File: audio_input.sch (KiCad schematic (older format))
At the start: 17 parts, among them U8 OPA1664

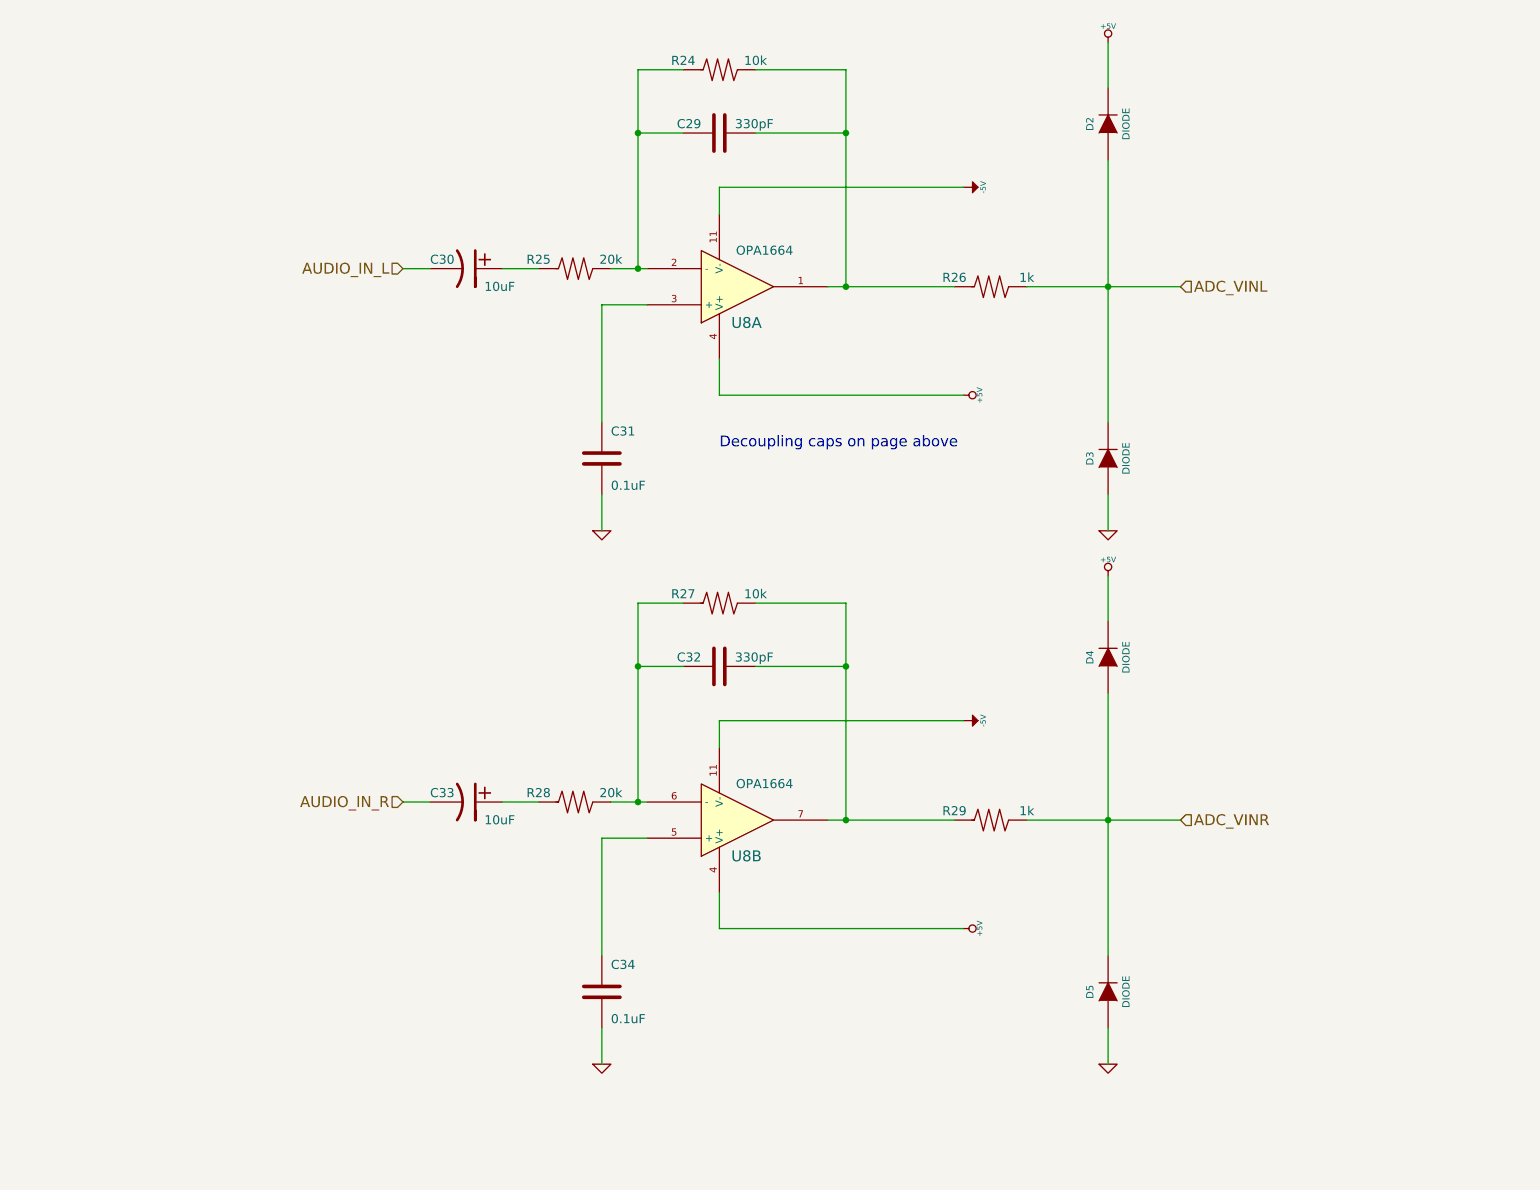
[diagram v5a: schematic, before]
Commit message: Fixed decoupling cap polarity on output op-amp, added bias to analog input, changed capacitor footprints to reflect new capacitor selections
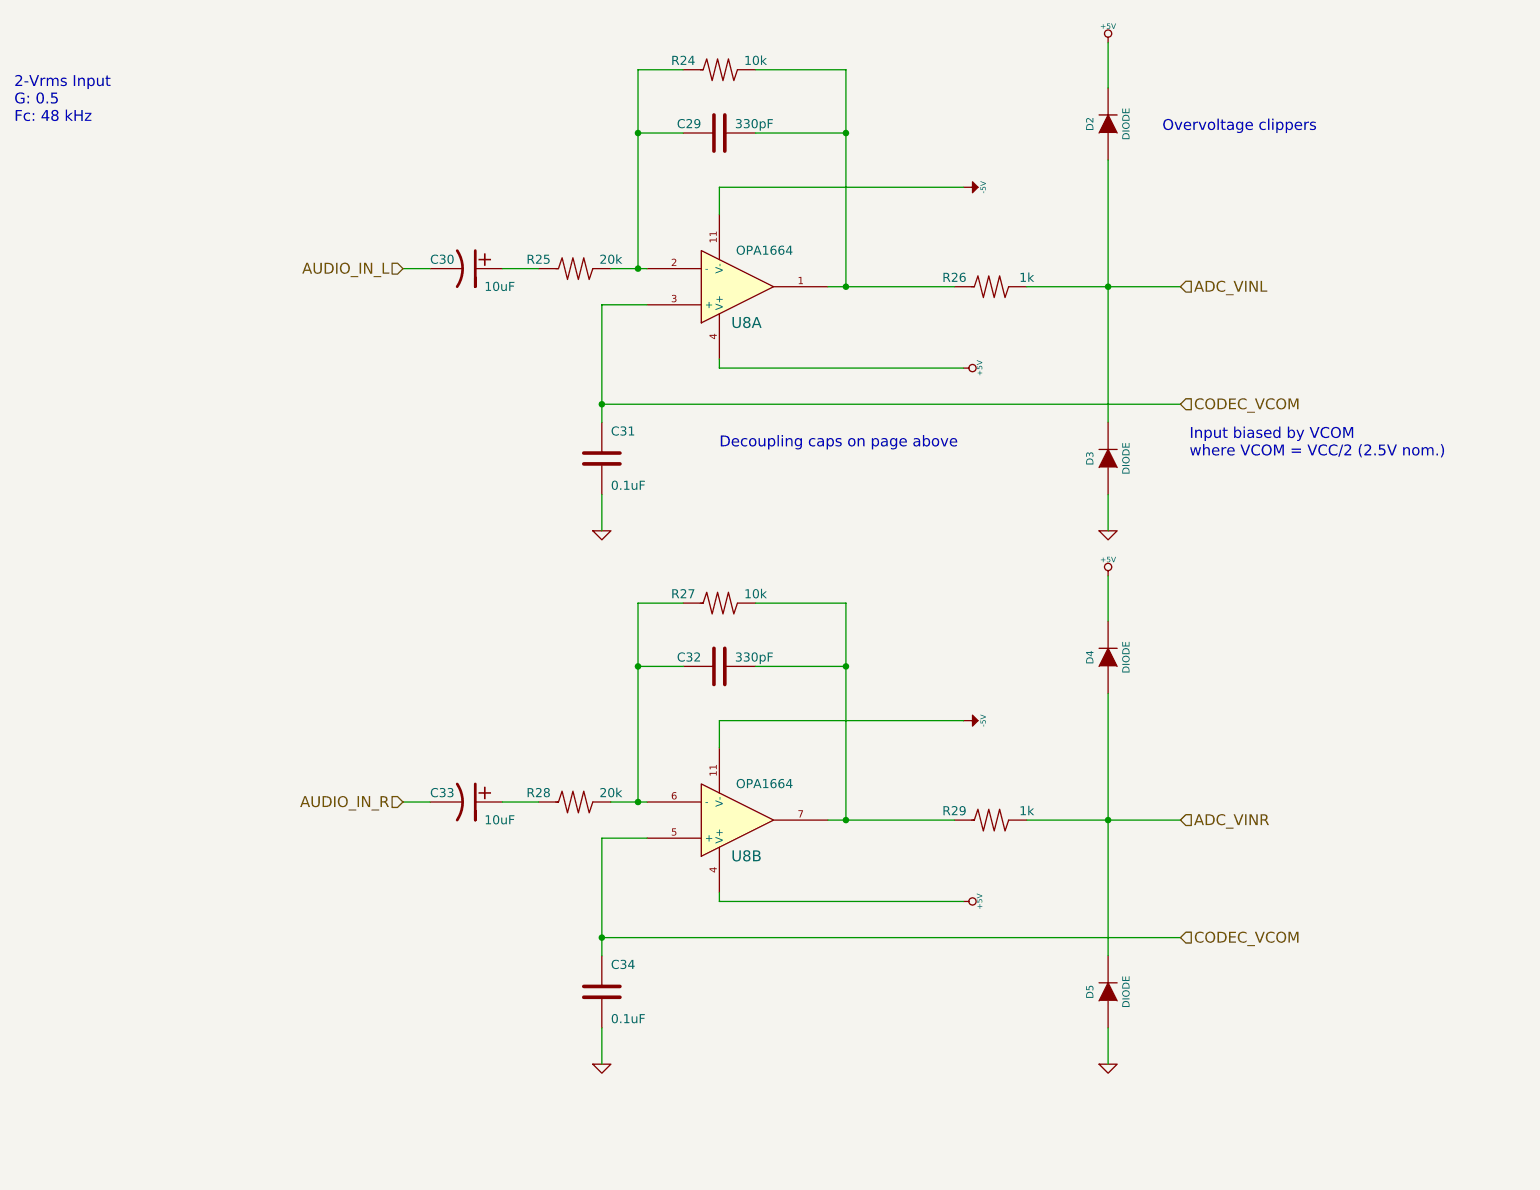
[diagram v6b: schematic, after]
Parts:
- C30, C33: footprint (none) -> Capacitors_SMD:c_elec_6.3x5.7
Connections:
- net CODEC_VCOM: now reaches C31.1, U8.3 (+)
- net CODEC_VCOM: now also C34.1, U8.5 (+)
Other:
- note added: "2-Vrms Input\nG: 0.5\nFc: 48 kHz"
- note added: "Input biased by VCOM \nwhere VCOM = VCC/2 (2.5V nom.)"
- note added: "Overvoltage clippers"
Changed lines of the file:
@@
 	1    0    0    1
 $EndComp
-Wire Wire Line
-	3250 2000 3400 2000
-Wire Wire Line
-	4400 2000 4600 2000
-Wire Wire Line
-	5000 1550 5000 1700
-$Comp
-L -5V #PWR88
+$Comp
+L -5V #PWR087
 U 1 1 5A49B7EA
 P 6350 1550
-F 0 "#PWR88" H 6350 1690 20  0001 C CNN
+F 0 "#PWR087" H 6350 1690 20  0001 C CNN
 F 1 "-5V" H 6350 1660 30  0000 C CNN
 F 2 "" H 6350 1550 60  0000 C CNN
@@
 	0    -1   -1   0
 $EndComp
-Wire Wire Line
-	4550 900  4550 2000
-Wire Wire Line
-	4550 1250 4800 1250
-Connection ~ 4550 2000
 $Comp
 L CP1 C30
@@
 F 0 "C30" V 3550 1800 50  0000 L CNN
 F 1 "10uF" V 3700 2100 50  0000 L CNN
-F 2 "" H 3600 2000 60  0001 C CNN
+F 2 "Capacitors_SMD:c_elec_6.3x5.7" H 3600 2000 60  0001 C CNN
 F 3 "" H 3600 2000 60  0000 C CNN
 	1    3600 2000
@@
 	1    0    0    -1
 $EndComp
-Wire Wire Line
-	4350 2850 4350 2200
-Wire Wire Line
-	4350 2200 4600 2200
-Wire Wire Line
-	5000 1550 6350 1550
-Wire Wire Line
-	5600 2100 6300 2100
-Wire Wire Line
-	5700 900  5700 2100
-Wire Wire Line
-	5700 1250 5200 1250
 $Comp
 L R R24
@@
 	1    0    0    -1
 $EndComp
-Wire Wire Line
-	4550 900  4800 900
-Connection ~ 4550 1250
-Wire Wire Line
-	5200 900  5700 900
-Connection ~ 5700 1250
-$Comp
-L GND #PWR90
+$Comp
+L GND #PWR088
 U 1 1 5A49BD8E
 P 4350 3450
-F 0 "#PWR90" H 4350 3450 30  0001 C CNN
+F 0 "#PWR088" H 4350 3450 30  0001 C CNN
 F 1 "GND" H 4350 3380 30  0001 C CNN
 F 2 "" H 4350 3450 60  0000 C CNN
@@
 	1    0    0    -1
 $EndComp
-Wire Wire Line
-	4350 3450 4350 3450
-Wire Wire Line
-	4350 3450 4350 3250
 $Comp
 L R R25
@@
 	1    0    0    -1
 $EndComp
-Wire Wire Line
-	4000 2000 3800 2000
 $Comp
 L R R26
@@
 	1    0    0    -1
 $EndComp
-Connection ~ 5700 2100
-Connection ~ 7150 2100
-Wire Wire Line
-	6700 2100 7550 2100
-Wire Wire Line
-	7150 1400 7150 2850
-Wire Wire Line
-	7150 750  7150 1000
-Wire Wire Line
-	7150 3450 7150 3250
-$Comp
-L GND #PWR91
+$Comp
+L GND #PWR089
 U 1 1 5A49C264
 P 7150 3450
-F 0 "#PWR91" H 7150 3450 30  0001 C CNN
+F 0 "#PWR089" H 7150 3450 30  0001 C CNN
 F 1 "GND" H 7150 3380 30  0001 C CNN
 F 2 "" H 7150 3450 60  0000 C CNN
@@
 $EndComp
 $Comp
-L +5V #PWR87
+L +5V #PWR090
 U 1 1 5A49C8EC
 P 7150 750
-F 0 "#PWR87" H 7150 840 20  0001 C CNN
+F 0 "#PWR090" H 7150 840 20  0001 C CNN
 F 1 "+5V" H 7150 840 30  0000 C CNN
 F 2 "" H 7150 750 60  0000 C CNN
@@
 	1    0    0    1
 $EndComp
-Wire Wire Line
-	3250 4950 3400 4950
-Wire Wire Line
-	4400 4950 4600 4950
-Wire Wire Line
-	5000 4500 5000 4650
-$Comp
-L -5V #PWR93
+$Comp
+L -5V #PWR091
 U 1 1 5A49EA7F
 P 6350 4500
-F 0 "#PWR93" H 6350 4640 20  0001 C CNN
+F 0 "#PWR091" H 6350 4640 20  0001 C CNN
 F 1 "-5V" H 6350 4610 30  0000 C CNN
 F 2 "" H 6350 4500 60  0000 C CNN
@@
 $EndComp
 $Comp
-L +5V #PWR94
+L +5V #PWR092
 U 1 1 5A49EA85
-P 6350 5650
-F 0 "#PWR94" H 6350 5740 20  0001 C CNN
-F 1 "+5V" H 6350 5740 30  0000 C CNN
-F 2 "" H 6350 5650 60  0000 C CNN
-F 3 "" H 6350 5650 60  0000 C CNN
-	1    6350 5650
+P 6350 5500
+F 0 "#PWR092" H 6350 5590 20  0001 C CNN
+F 1 "+5V" H 6350 5590 30  0000 C CNN
+F 2 "" H 6350 5500 60  0000 C CNN
+F 3 "" H 6350 5500 60  0000 C CNN
+	1    6350 5500
 	0    1    1    0
 $EndComp
@@
 	0    -1   -1   0
 $EndComp
-Wire Wire Line
-	4550 3850 4550 4950
-Wire Wire Line
-	4550 4200 4800 4200
-Connection ~ 4550 4950
 $Comp
 L CP1 C33
@@
 F 0 "C33" V 3550 4750 50  0000 L CNN
 F 1 "10uF" V 3700 5050 50  0000 L CNN
-F 2 "" H 3600 4950 60  0001 C CNN
+F 2 "Capacitors_SMD:c_elec_6.3x5.7" H 3600 4950 60  0001 C CNN
 F 3 "" H 3600 4950 60  0000 C CNN
 	1    3600 4950
@@
 	1    0    0    -1
 $EndComp
-Wire Wire Line
-	4350 5800 4350 5150
-Wire Wire Line
-	4350 5150 4600 5150
-Wire Wire Line
-	5000 5650 6350 5650
-Wire Wire Line
-	5000 4500 6350 4500
-Wire Wire Line
-	5600 5050 6300 5050
-Wire Wire Line
-	5700 3850 5700 5050
-Wire Wire Line
-	5700 4200 5200 4200
 $Comp
 L R R27
@@
 	1    0    0    -1
 $EndComp
-Wire Wire Line
-	4550 3850 4800 3850
-Connection ~ 4550 4200
-Wire Wire Line
-	5200 3850 5700 3850
-Connection ~ 5700 4200
-$Comp
-L GND #PWR95
+$Comp
+L GND #PWR093
 U 1 1 5A49EAC6
 P 4350 6400
-F 0 "#PWR95" H 4350 6400 30  0001 C CNN
+F 0 "#PWR093" H 4350 6400 30  0001 C CNN
 F 1 "GND" H 4350 6330 30  0001 C CNN
 F 2 "" H 4350 6400 60  0000 C CNN
@@
 	1    0    0    -1
 $EndComp
-Wire Wire Line
-	4350 6400 4350 6400
-Wire Wire Line
-	4350 6400 4350 6200
 $Comp
 L R R28
@@
 	1    0    0    -1
 $EndComp
-Wire Wire Line
-	4000 4950 3800 4950
 $Comp
 L R R29
@@
 	1    0    0    -1
 $EndComp
-Connection ~ 5700 5050
-Connection ~ 7150 5050
-Wire Wire Line
-	6700 5050 7550 5050
-Wire Wire Line
-	7150 4350 7150 5800
-Wire Wire Line
-	7150 3700 7150 3950
-Wire Wire Line
-	7150 6400 7150 6200
-$Comp
-L GND #PWR96
+$Comp
+L GND #PWR094
 U 1 1 5A49EAF1
 P 7150 6400
-F 0 "#PWR96" H 7150 6400 30  0001 C CNN
+F 0 "#PWR094" H 7150 6400 30  0001 C CNN
 F 1 "GND" H 7150 6330 30  0001 C CNN
 F 2 "" H 7150 6400 60  0000 C CNN
@@
 $EndComp
 $Comp
-L +5V #PWR92
+L +5V #PWR095
 U 1 1 5A49EB03
 P 7150 3700
-F 0 "#PWR92" H 7150 3790 20  0001 C CNN
+F 0 "#PWR095" H 7150 3790 20  0001 C CNN
 F 1 "+5V" H 7150 3790 30  0000 C CNN
 F 2 "" H 7150 3700 60  0000 C CNN
@@
 Text Notes 5000 3000 0    60   ~ 0
 Decoupling caps on page above
-Wire Wire Line
-	5000 2700 6350 2700
-$Comp
-L +5V #PWR89
+$Comp
+L +5V #PWR096
 U 1 1 5A49B806
-P 6350 2700
-F 0 "#PWR89" H 6350 2790 20  0001 C CNN
-F 1 "+5V" H 6350 2790 30  0000 C CNN
-F 2 "" H 6350 2700 60  0000 C CNN
-F 3 "" H 6350 2700 60  0000 C CNN
-	1    6350 2700
-	0    1    1    0
-$EndComp
-Wire Wire Line
-	5000 2700 5000 2500
-Wire Wire Line
-	5000 5650 5000 5450
+P 6350 2550
+F 0 "#PWR096" H 6350 2640 20  0001 C CNN
+F 1 "+5V" H 6350 2640 30  0000 C CNN
+F 2 "" H 6350 2550 60  0000 C CNN
+F 3 "" H 6350 2550 60  0000 C CNN
+	1    6350 2550
+	0    1    1    0
+$EndComp
+Text Notes 1100 1200 0    60   ~ 0
+2-Vrms Input\nG: 0.5\nFc: 48 kHz
+Text Notes 7450 1250 0    60   ~ 0
+Overvoltage clippers
+Wire Wire Line
+	3250 2000 3400 2000
+Wire Wire Line
+	4400 2000 4600 2000
+Wire Wire Line
+	5000 1550 5000 1700
+Wire Wire Line
+	4550 900  4550 2000
+Wire Wire Line
+	4550 1250 4800 1250
+Connection ~ 4550 2000
+Wire Wire Line
+	4350 2850 4350 2200
+Wire Wire Line
+	4350 2200 4600 2200
+Wire Wire Line
+	5000 1550 6350 1550
+Wire Wire Line
+	5600 2100 6300 2100
+Wire Wire Line
+	5700 900  5700 2100
+Wire Wire Line
+	5700 1250 5200 1250
+Wire Wire Line
+	4550 900  4800 900
+Connection ~ 4550 1250
+Wire Wire Line
+	5200 900  5700 900
+Connection ~ 5700 1250
+Wire Wire Line
+	4350 3450 4350 3450
+Wire Wire Line
+	4350 3450 4350 3250
+Wire Wire Line
+	4000 2000 3800 2000
+Connection ~ 5700 2100
+Connection ~ 7150 2100
+Wire Wire Line
+	6700 2100 7550 2100
+Wire Wire Line
+	7150 1400 7150 2850
+Wire Wire Line
+	7150 750  7150 1000
+Wire Wire Line
+	7150 3450 7150 3250
+Wire Wire Line
+	3250 4950 3400 4950
+Wire Wire Line
+	4400 4950 4600 4950
+Wire Wire Line
+	5000 4500 5000 4650
+Wire Wire Line
+	4550 3850 4550 4950
+Wire Wire Line
+	4550 4200 4800 4200
+Connection ~ 4550 4950
+Wire Wire Line
+	4350 5800 4350 5150
+Wire Wire Line
+	4350 5150 4600 5150
+Wire Wire Line
+	5000 5500 6350 5500
+Wire Wire Line
+	5000 4500 6350 4500
+Wire Wire Line
+	5600 5050 6300 5050
+Wire Wire Line
+	5700 3850 5700 5050
+Wire Wire Line
+	5700 4200 5200 4200
+Wire Wire Line
+	4550 3850 4800 3850
+Connection ~ 4550 4200
+Wire Wire Line
+	5200 3850 5700 3850
+Connection ~ 5700 4200
+Wire Wire Line
+	4350 6400 4350 6400
+Wire Wire Line
+	4350 6400 4350 6200
+Wire Wire Line
+	4000 4950 3800 4950
+Connection ~ 5700 5050
+Connection ~ 7150 5050
+Wire Wire Line
+	6700 5050 7550 5050
+Wire Wire Line
+	7150 4350 7150 5800
+Wire Wire Line
+	7150 3700 7150 3950
+Wire Wire Line
+	7150 6400 7150 6200
+Wire Wire Line
+	5000 2550 6350 2550
+Wire Wire Line
+	5000 2550 5000 2500
+Wire Wire Line
+	5000 5500 5000 5450
+Text HLabel 7550 2750 2    60   Input ~ 0
+CODEC_VCOM
+Wire Wire Line
+	7550 2750 4350 2750
+Connection ~ 4350 2750
+Text HLabel 7550 5700 2    60   Input ~ 0
+CODEC_VCOM
+Wire Wire Line
+	7550 5700 4350 5700
+Connection ~ 4350 5700
+Text Notes 7600 3050 0    60   ~ 0
+Input biased by VCOM \nwhere VCOM = VCC/2 (2.5V nom.)
 $EndSCHEMATC

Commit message: Updated audio capacitor types to reflect BOM
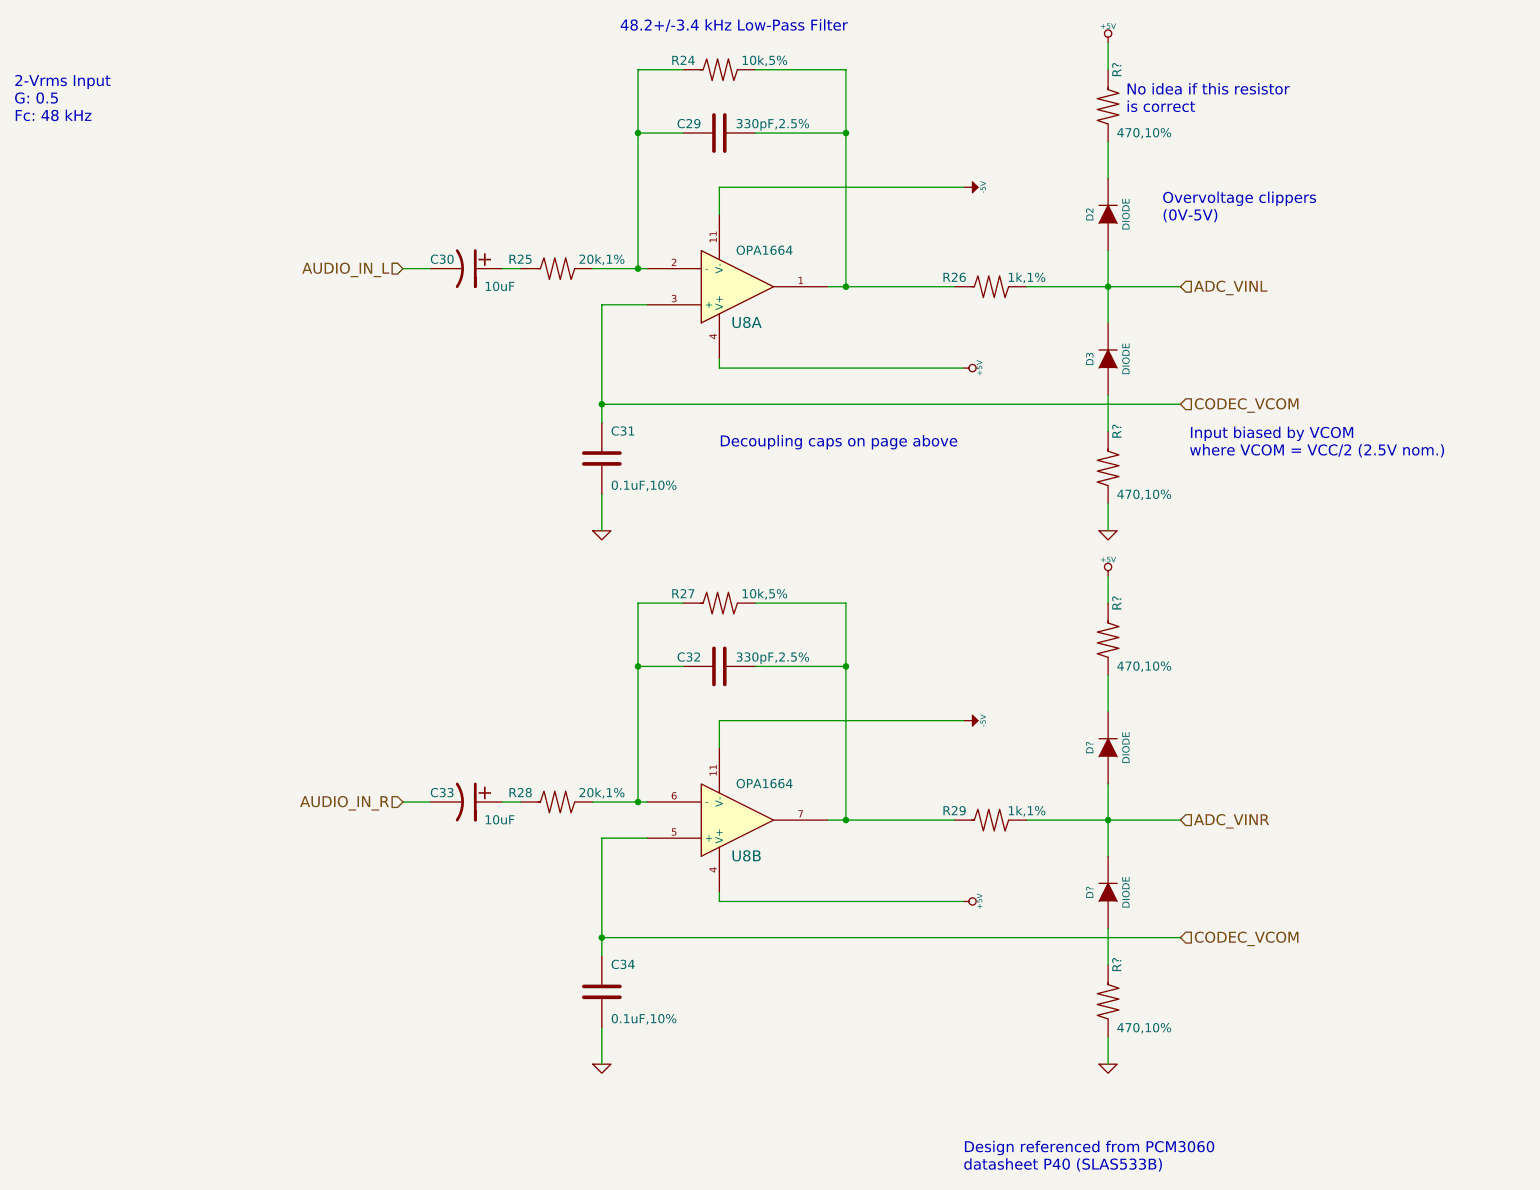
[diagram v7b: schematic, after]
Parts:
- removed D4, D5: DIODE, symbol DIODE
- added D? (x2): DIODE, symbol DIODE
- added R? (x4): 470,10%, symbol R
- C29, C32: value 330pF -> 330pF,2.5%; footprint (none) -> muse-v3:C_Rect_L7.2_W4.5_P5
- C31, C34: value 0.1uF -> 0.1uF,10%; footprint (none) -> Capacitors_THT:C_Rect_L18_W11_H19_P15
- R24, R27: value 10k -> 10k,5%
- R25, R28: value 20k -> 20k,1%
- R26, R29: value 1k -> 1k,1%
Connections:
- net +5V: now also R?.2, R?.2; no longer D2.2 (K)
- net ADC_VINR: now also D?.1 (A), D?.2 (K)
- net GND: now also R?.1, R?.1; no longer D3.1 (A)
- new net: D3.1 (A), R?.2
- new net: D2.2 (K), R?.1
- new net: D?.1 (A), R?.2
- new net: D?.2 (K), R?.1
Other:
- note added: "48.2+/-3.4 kHz Low-Pass Filter"
- note added: "Design referenced from PCM3060\ndatasheet P40 (SLAS533B)"
- note added: "No idea if this resistor\nis correct"
- note added: "Overvoltage clippers \n(0V-5V)"
- note removed: "Overvoltage clippers"
- moved on the sheet: D2, D3, R25, R28
